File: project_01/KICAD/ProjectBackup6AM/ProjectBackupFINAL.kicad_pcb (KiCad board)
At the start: 2 copper layers, 52 x 50.8 mm, 45 parts, among them J2 UJ20-C-H-G-SMT-1-P16-TR, Q5 BSS138, Q7 BSS138, SW1 Boot, SW2 RST, U1 TPB4056A20-ES1R, U2 DRV5032FADBZR, U3 TPS613222ADBVR, U5 XC6206P332MR-G, U6 ESP32-S3-WROOM-1-N16R8

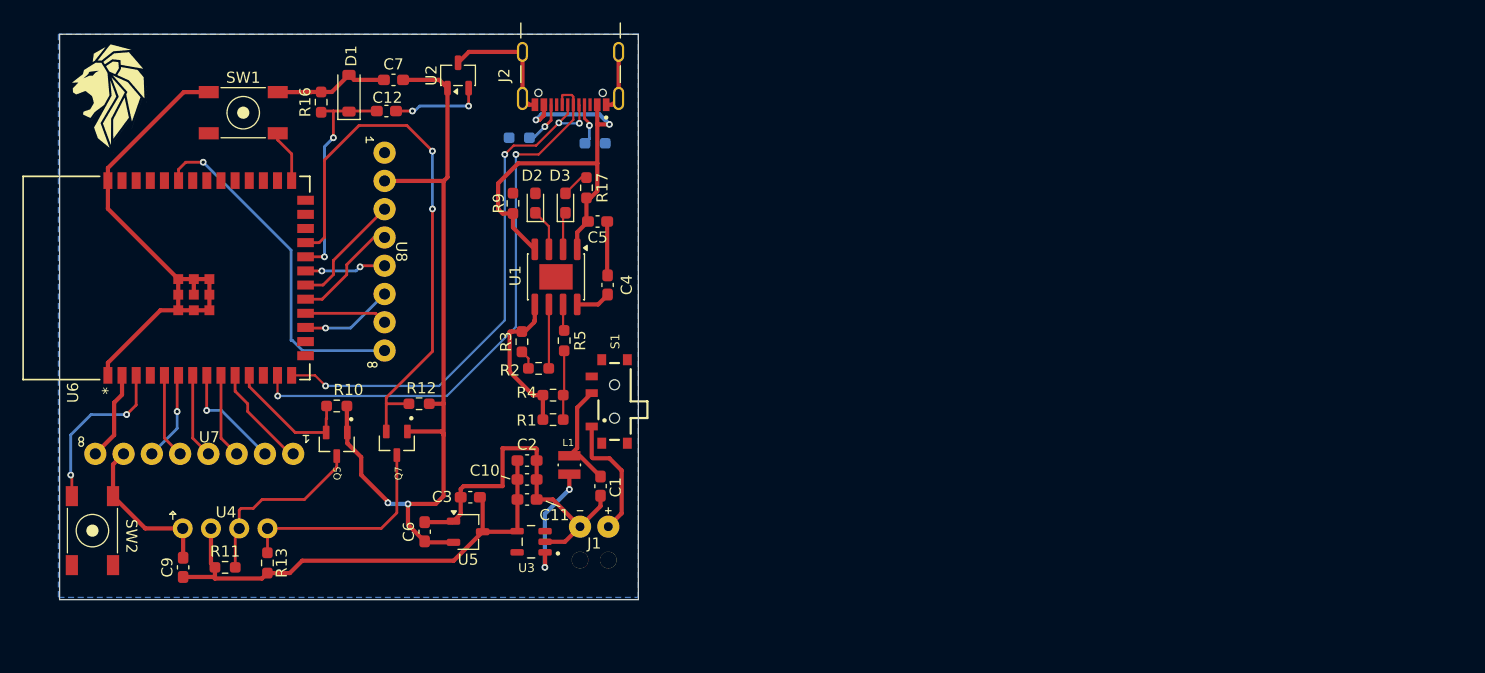
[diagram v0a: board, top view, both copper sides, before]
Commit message: Update KiCad schematics to v10; clean backups
Bump KiCad schematic version/generator to v10 and normalize symbol/property metadata in Boost5V.kicad_sch (add show_name/do_not_autoplace/hide/in_pos_files, standardize pin names/numbers/types and orientations). Apply similar component property adjustments (e.g. TPB4056, XC6206, TPS613222) and update related project PCB/PRO/PRL/SCH files. Add ProjectBackupFINAL and several new zip backups, and remove many old backup, cache and lock files to clean up the repository. These are primarily metadata and housekeeping changes, not functional circuit edits.
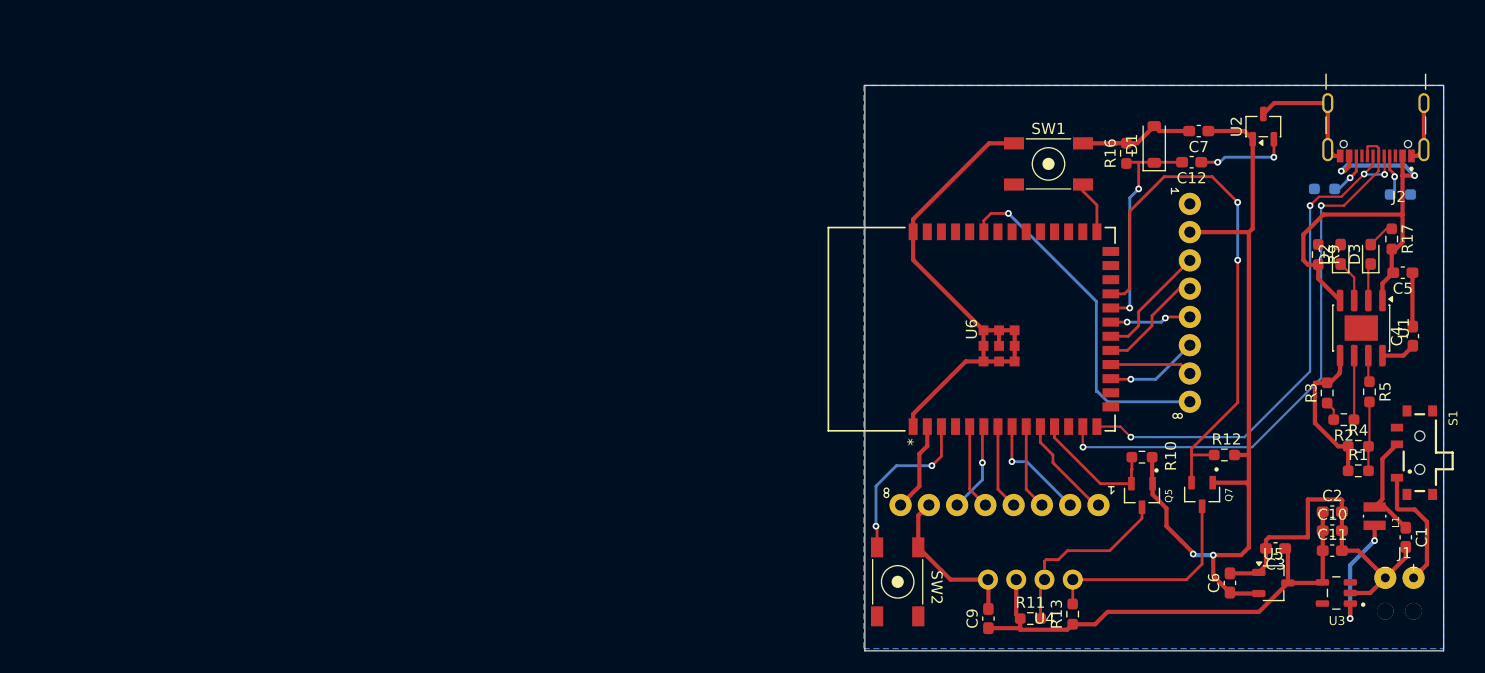
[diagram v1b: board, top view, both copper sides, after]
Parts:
- removed G***: LOGO, LOGO
- moved C10 72.5 mm to (142.4, 65.4)
- moved C11 72.5 mm to (142.4, 67.2)
- moved C2 72.5 mm to (142.4, 63.7)
- moved C3 72.5 mm to (137.3, 67.0)
- moved C5 72.5 mm to (148.7, 42.2)
- moved C7 72.5 mm to (130.4, 29.5)
- moved D1 72.5 mm to (126.4, 30.7)
- moved D2 72.5 mm to (143.2, 40.6)
- moved R1 72.5 mm to (144.7, 60.0)
- moved R16 72.5 mm to (123.9, 31.5)
- moved R17 72.5 mm to (147.7, 39.2)
- moved R2 72.5 mm to (143.4, 55.4)
- moved R3 72.5 mm to (141.9, 53.0)
- moved R4 72.5 mm to (144.7, 57.8)
- moved R5 72.5 mm to (145.7, 52.9)
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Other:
- board text added: "ESP32-S3-N16R8"
- board text added: "LogicLevelConverter"
- board text added: "Main Sheet"
- board text added: "Power Circuitry"
- board text added: "USBC-CONN"
- board text removed: "Dotted outline is size of the keyboard, and thus minimum size of the device. The difference between the keyboard size and the PCB size, that negative space, will be where the LiPo battery sits."
- board text removed: "LiPo"
